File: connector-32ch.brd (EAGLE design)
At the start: 26.7 x 25.4 mm, 67 parts, among them X1 OMNETICS_36PAD

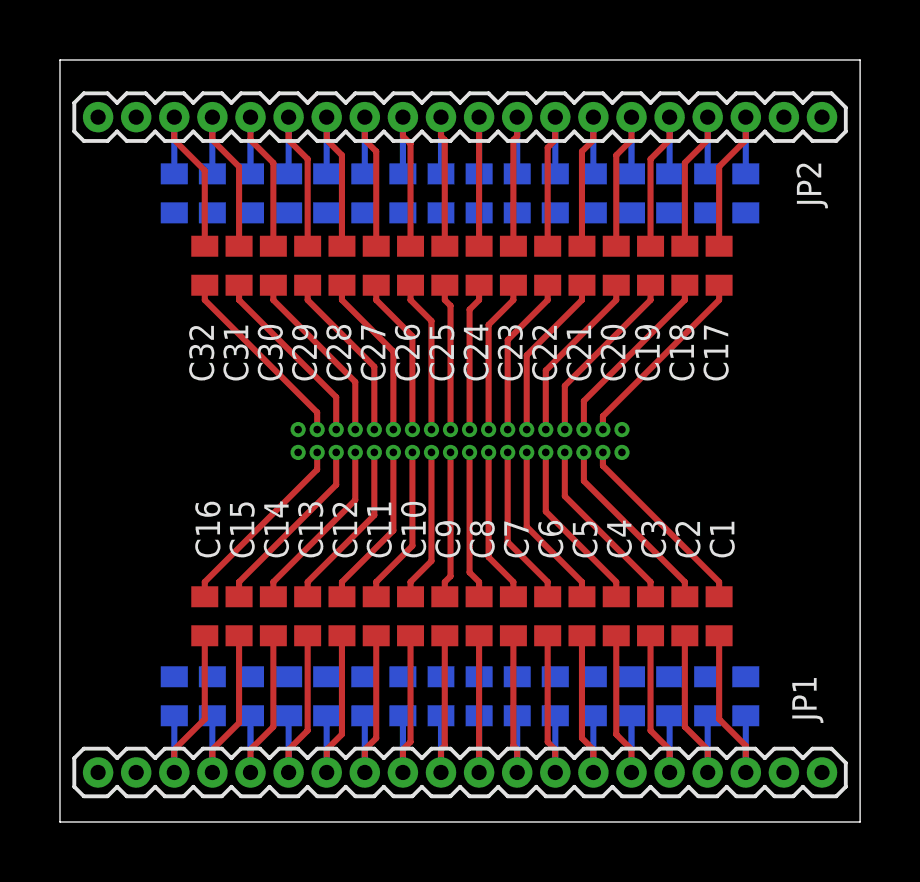
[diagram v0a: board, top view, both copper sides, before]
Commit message: finished neural connector board.
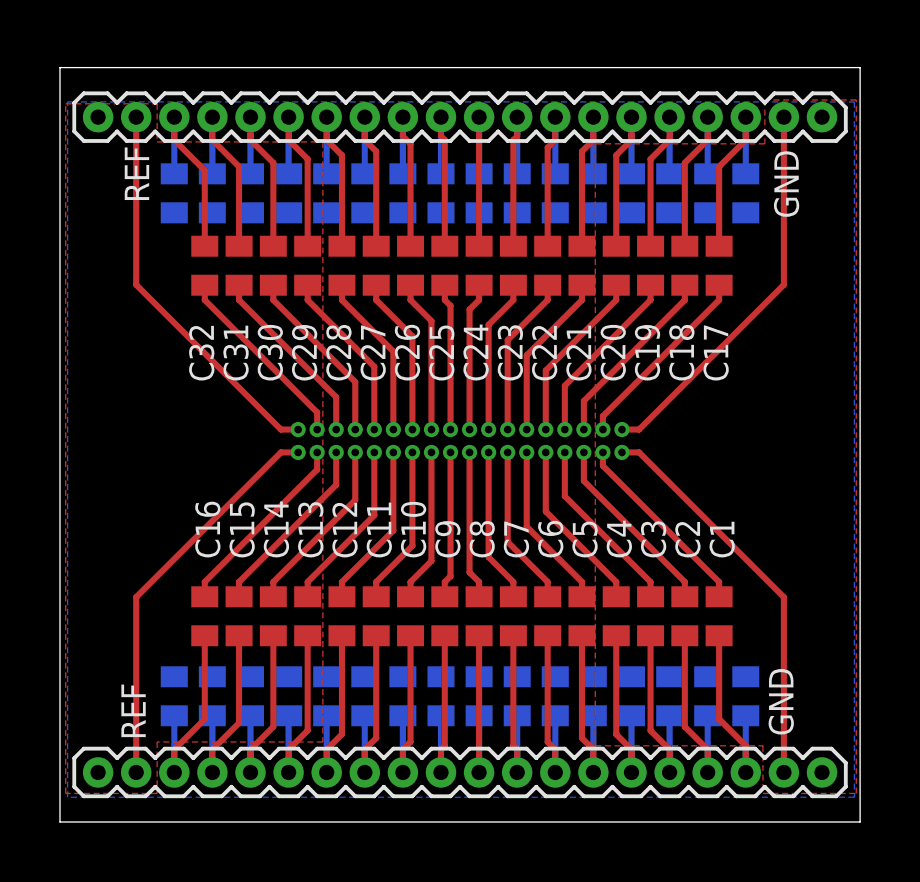
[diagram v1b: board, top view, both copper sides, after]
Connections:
- removed net N$65: R1.2, R2.2, R3.2, R4.2, R5.2, R6.2, R7.2, R8.2
- removed net N$66: R17.2, R18.2, R19.2, R20.2, R21.2, R22.2, R23.2, R24.2
- removed net N$67: R10.1, R11.1, R12.1, R13.1, R14.1, R15.1, R16.1, R9.1
- removed net N$68: R25.1, R26.1, R27.1, R28.1, R29.1, R30.1, R31.1, R32.1
- new net G: JP1.19, JP2.19, X1.G1, X1.R2
- new net R: JP1.2, JP2.2, X1.G2, X1.R1
- new net VCM: JP1.1, JP1.20, JP2.1, JP2.20, R1.2, R10.1, R11.1, R12.1, R13.1, R14.1, R15.1, R16.1, R17.2, R18.2, R19.2, R2.2, R20.2, R21.2, R22.2, R23.2, R24.2, R25.1, R26.1, R27.1, R28.1, R29.1, R3.2, R30.1, R31.1, R32.1, R4.2, R5.2, R6.2, R7.2, R8.2, R9.1
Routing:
- net G: track 0.00 -> 26.2 mm
- net R: track 0.00 -> 26.2 mm
- added copper zone on layer 1, net G
- added copper zone on layer 1, net R
- added copper zone on layer 16, net VCM
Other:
- board size 26.7 x 25.4 mm -> 26.7 x 25.1 mm
- board text added: "GND"
- board text added: "REF"
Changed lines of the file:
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@@
 <setting verticaltext="up"/>
 </settings>
-<grid distance="0.005" unitdist="inch" unit="mm" style="lines" multiple="1" display="yes" altdistance="0.025" altunitdist="inch" altunit="inch"/>
+<grid distance="0.0025" unitdist="inch" unit="inch" style="lines" multiple="1" display="yes" altdistance="0.025" altunitdist="inch" altunit="inch"/>
 <layers>
 <layer number="1" name="Top" color="4" fill="1" visible="yes" active="yes"/>
@@
 <plain>
 <wire x1="0" y1="0" x2="26.67" y2="0" width="0" layer="20"/>
-<wire x1="26.67" y1="0" x2="26.67" y2="25.4" width="0" layer="20"/>
-<wire x1="26.67" y1="25.4" x2="0" y2="25.4" width="0" layer="20"/>
-<wire x1="0" y1="25.4" x2="0" y2="0" width="0" layer="20"/>
+<wire x1="26.67" y1="0" x2="26.67" y2="25.146" width="0" layer="20"/>
+<wire x1="26.67" y1="25.146" x2="0" y2="25.146" width="0" layer="20"/>
+<wire x1="0" y1="25.146" x2="0" y2="0" width="0" layer="20"/>
+<text x="2.159" y="22.5425" size="0.8128" layer="25" rot="R270">REF</text>
+<text x="2.8575" y="2.7305" size="0.8128" layer="25" font="fixed" rot="R90">REF</text>
+<text x="24.4475" y="2.8575" size="0.8128" layer="25" font="fixed" rot="R90">GND</text>
+<text x="23.8125" y="22.4155" size="0.8128" layer="25" font="fixed" rot="R270">GND</text>
 </plain>
 <attributes>
@@
 <attribute name="VALUE" x="1.905" y="20.32" size="1.27" layer="28" rot="MR90"/>
 </element>
-<element name="JP1" library="mor307" package="1X20" value="M20" x="25.4" y="1.651" smashed="yes" rot="R180">
-<attribute name="NAME" x="25.2222" y="3.3528" size="0.8128" layer="25" ratio="10" rot="R90"/>
-</element>
-<element name="JP2" library="mor307" package="1X20" value="M20" x="25.4" y="23.495" smashed="yes" rot="R180">
-<attribute name="NAME" x="24.5618" y="22.0472" size="0.8128" layer="25" ratio="10" rot="R270"/>
-</element>
+<element name="JP1" library="mor307" package="1X20" value="M20" x="25.4" y="1.651" smashed="yes" rot="R180"/>
+<element name="JP2" library="mor307" package="1X20" value="M20" x="25.4" y="23.495" smashed="yes" rot="R180"/>
 </elements>
 <signals>
@@
 <wire x1="3.81" y1="21.605" x2="3.81" y2="23.495" width="0.2032" layer="16"/>
 </signal>
-<signal name="N$65">
+<signal name="VCM">
 <contactref element="R1" pad="2"/>
 <contactref element="R8" pad="2"/>
@@
 <contactref element="R3" pad="2"/>
 <contactref element="R2" pad="2"/>
-<wire x1="21.59" y1="4.841" x2="22.86" y2="4.841" width="0" layer="19" extent="16-16"/>
-<wire x1="20.32" y1="4.841" x2="21.59" y2="4.841" width="0" layer="19" extent="16-16"/>
-<wire x1="19.05" y1="4.841" x2="20.32" y2="4.841" width="0" layer="19" extent="16-16"/>
-<wire x1="17.78" y1="4.841" x2="19.05" y2="4.841" width="0" layer="19" extent="16-16"/>
-<wire x1="16.51" y1="4.841" x2="17.78" y2="4.841" width="0" layer="19" extent="16-16"/>
-<wire x1="15.24" y1="4.841" x2="16.51" y2="4.841" width="0" layer="19" extent="16-16"/>
-<wire x1="13.97" y1="4.841" x2="15.24" y2="4.841" width="0" layer="19" extent="16-16"/>
-</signal>
-<signal name="N$66">
+<contactref element="JP1" pad="1"/>
 <contactref element="R24" pad="2"/>
 <contactref element="R17" pad="2"/>
@@
 <contactref element="R22" pad="2"/>
 <contactref element="R23" pad="2"/>
-<wire x1="21.59" y1="20.305" x2="22.86" y2="20.305" width="0" layer="19" extent="16-16"/>
-<wire x1="20.32" y1="20.305" x2="21.59" y2="20.305" width="0" layer="19" extent="16-16"/>
-<wire x1="19.05" y1="20.305" x2="20.32" y2="20.305" width="0" layer="19" extent="16-16"/>
-<wire x1="17.78" y1="20.305" x2="19.05" y2="20.305" width="0" layer="19" extent="16-16"/>
-<wire x1="16.51" y1="20.305" x2="17.78" y2="20.305" width="0" layer="19" extent="16-16"/>
-<wire x1="15.24" y1="20.305" x2="16.51" y2="20.305" width="0" layer="19" extent="16-16"/>
-<wire x1="13.97" y1="20.305" x2="15.24" y2="20.305" width="0" layer="19" extent="16-16"/>
-</signal>
-<signal name="N$67">
+<contactref element="JP2" pad="1"/>
 <contactref element="R16" pad="1"/>
 <contactref element="R9" pad="1"/>
@@
 <contactref element="R11" pad="1"/>
 <contactref element="R10" pad="1"/>
-<wire x1="11.43" y1="4.841" x2="12.7" y2="4.841" width="0" layer="19" extent="16-16"/>
-<wire x1="10.16" y1="4.841" x2="11.43" y2="4.841" width="0" layer="19" extent="16-16"/>
-<wire x1="8.89" y1="4.841" x2="10.16" y2="4.841" width="0" layer="19" extent="16-16"/>
-<wire x1="7.62" y1="4.841" x2="8.89" y2="4.841" width="0" layer="19" extent="16-16"/>
-<wire x1="6.35" y1="4.841" x2="7.62" y2="4.841" width="0" layer="19" extent="16-16"/>
-<wire x1="5.08" y1="4.841" x2="6.35" y2="4.841" width="0" layer="19" extent="16-16"/>
-<wire x1="3.81" y1="4.841" x2="5.08" y2="4.841" width="0" layer="19" extent="16-16"/>
-</signal>
-<signal name="N$68">
+<contactref element="JP1" pad="20"/>
 <contactref element="R25" pad="1"/>
 <contactref element="R32" pad="1"/>
@@
 <contactref element="R27" pad="1"/>
 <contactref element="R26" pad="1"/>
-<wire x1="11.43" y1="20.305" x2="12.7" y2="20.305" width="0" layer="19" extent="16-16"/>
-<wire x1="10.16" y1="20.305" x2="11.43" y2="20.305" width="0" layer="19" extent="16-16"/>
-<wire x1="8.89" y1="20.305" x2="10.16" y2="20.305" width="0" layer="19" extent="16-16"/>
-<wire x1="7.62" y1="20.305" x2="8.89" y2="20.305" width="0" layer="19" extent="16-16"/>
-<wire x1="6.35" y1="20.305" x2="7.62" y2="20.305" width="0" layer="19" extent="16-16"/>
-<wire x1="5.08" y1="20.305" x2="6.35" y2="20.305" width="0" layer="19" extent="16-16"/>
-<wire x1="3.81" y1="20.305" x2="5.08" y2="20.305" width="0" layer="19" extent="16-16"/>
+<contactref element="JP2" pad="20"/>
+<polygon width="0.2032" layer="16">
+<vertex x="0.381" y="24.003"/>
+<vertex x="26.4795" y="24.003"/>
+<vertex x="26.4795" y="0.8255"/>
+<vertex x="0.254" y="0.8255"/>
+<vertex x="0.254" y="24.003"/>
+<vertex x="0.3175" y="24.003"/>
+</polygon>
+</signal>
+<signal name="R">
+<contactref element="X1" pad="R1"/>
+<contactref element="JP1" pad="2"/>
+<wire x1="24.13" y1="1.651" x2="24.13" y2="7.493" width="0.2032" layer="1"/>
+<wire x1="24.13" y1="7.493" x2="19.304" y2="12.319" width="0.2032" layer="1"/>
+<wire x1="19.304" y1="12.319" x2="18.7325" y2="12.319" width="0.2032" layer="1"/>
+<contactref element="X1" pad="G2"/>
+<contactref element="JP2" pad="2"/>
+<wire x1="24.13" y1="23.495" x2="24.13" y2="17.907" width="0.2032" layer="1"/>
+<wire x1="24.13" y1="17.907" x2="19.304" y2="13.081" width="0.2032" layer="1"/>
+<wire x1="19.304" y1="13.081" x2="18.7325" y2="13.081" width="0.2032" layer="1"/>
+<polygon width="0.2032" layer="1">
+<vertex x="26.543" y="24.0665"/>
+<vertex x="23.495" y="24.0665"/>
+<vertex x="23.495" y="22.606"/>
+<vertex x="17.8435" y="22.606"/>
+<vertex x="17.8435" y="2.54"/>
+<vertex x="23.4315" y="2.54"/>
+<vertex x="23.4315" y="0.9525"/>
+<vertex x="26.543" y="0.9525"/>
+</polygon>
+</signal>
+<signal name="G">
+<contactref element="X1" pad="R2"/>
+<contactref element="JP2" pad="19"/>
+<wire x1="2.54" y1="23.495" x2="2.54" y2="17.907" width="0.2032" layer="1"/>
+<wire x1="2.54" y1="17.907" x2="7.366" y2="13.081" width="0.2032" layer="1"/>
+<wire x1="7.366" y1="13.081" x2="7.9375" y2="13.081" width="0.2032" layer="1"/>
+<contactref element="X1" pad="G1"/>
+<contactref element="JP1" pad="19"/>
+<wire x1="2.54" y1="1.651" x2="2.54" y2="7.493" width="0.2032" layer="1"/>
+<wire x1="2.54" y1="7.493" x2="7.366" y2="12.319" width="0.2032" layer="1"/>
+<wire x1="7.366" y1="12.319" x2="7.9375" y2="12.319" width="0.2032" layer="1"/>
+<polygon width="0.2032" layer="1">
+<vertex x="0.1905" y="23.9395"/>
+<vertex x="3.2385" y="23.9395"/>
+<vertex x="3.2385" y="22.6695"/>
+<vertex x="8.763" y="22.6695"/>
+<vertex x="8.763" y="2.667"/>
+<vertex x="3.2385" y="2.667"/>
+<vertex x="3.2385" y="0.9525"/>
+<vertex x="0.1905" y="0.9525"/>
+</polygon>
 </signal>
 </signals>
